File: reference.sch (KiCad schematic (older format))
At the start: 8 parts, among them U6 REF5040, U7 REF5050

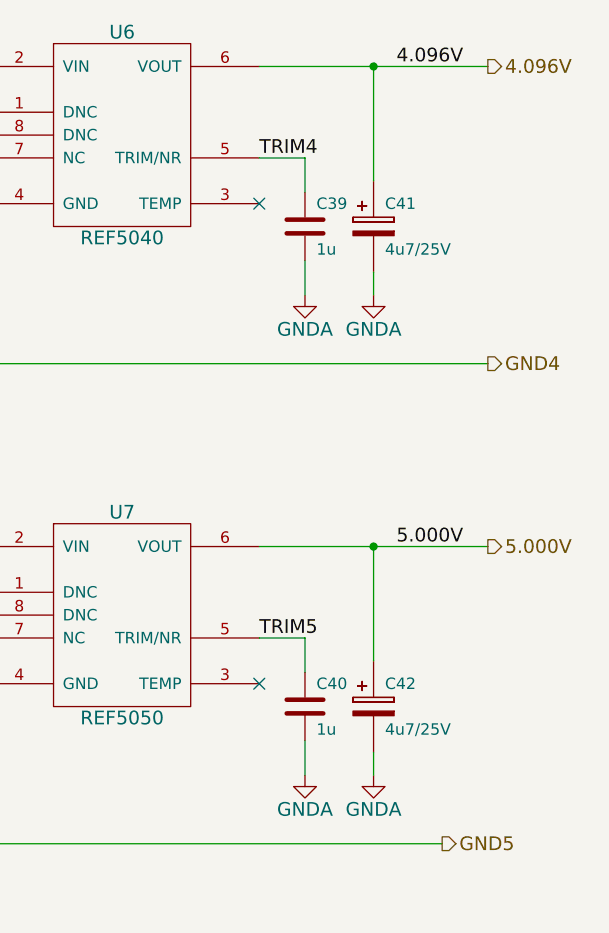
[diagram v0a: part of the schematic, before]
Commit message: Updated all part descriptions
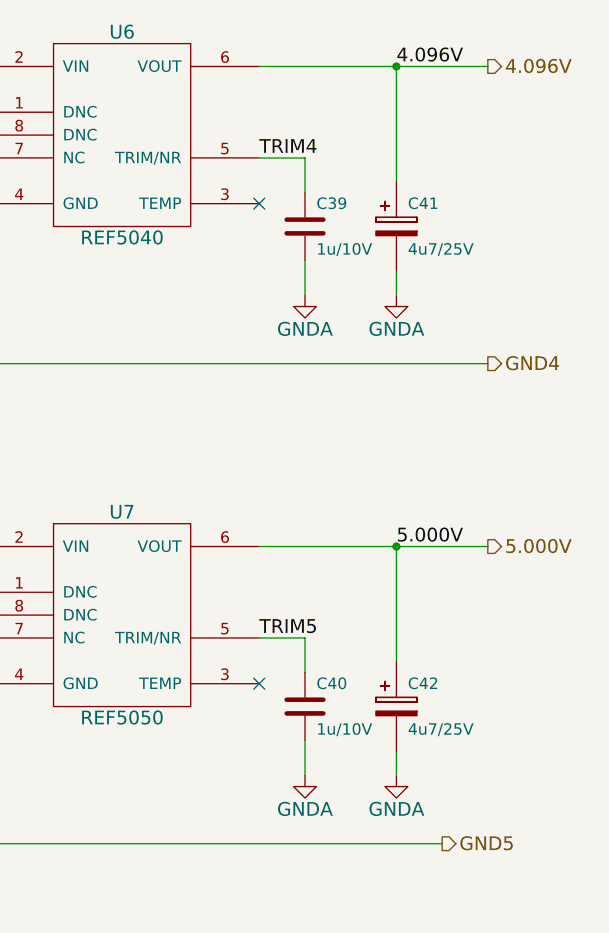
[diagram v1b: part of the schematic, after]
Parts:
- C37, C38, C41, C42: Alt. Order Code (none) -> 74-TR3B475K025C0700; Alt. Supplier (none) -> Mouser; Note (none) -> 4.7μ/25V/0.7Ω ESR case B tantalum capacitor; Package (none) -> case B; Supplier (none) -> Farnell
- C39, C40: value 1u -> 1u/10V; Alt. Order Code (none) -> 710-885012106010; Alt. Supplier (none) -> Mouser; Note (none) -> 1μF/10V X5R 0603 ceramic capacitor; Package (none) -> 0603; Supplier (none) -> Farnell
- U6: Alt. Order Code (none) -> 595-REF5040AIDGKT; Alt. Supplier (none) -> Mouser; Note (none) -> 5.000V low-noise very low drift precision voltage reference; Package (none) -> MSOP-8; Supplier (none) -> Farnell
- U7: Alt. Order Code (none) -> 595-REF5050AIDGKT; Alt. Supplier (none) -> Mouser; Note (none) -> 4.096V low-noise very low drift precision voltage reference; Package (none) -> MSOP-8; Supplier (none) -> Farnell
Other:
- moved on the sheet: C41, C42
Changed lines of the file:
@@
 EESchema Schematic File Version 2
-LIBS:MicroFLiC_DAC_1_0-rescue
 LIBS:power
 LIBS:device
@@
 LIBS:valves
 LIBS:jakub
-LIBS:MicroFLiC_DAC_1_0-cache
+LIBS:MicroFLiC_DAC-cache
 EELAYER 25 0
 EELAYER END
@@
 F 4 "REF5040AIDGKT" H 4100 2300 60  0001 C CNN "Part Number"
 F 5 "Texas Instruments" H 4100 2300 60  0001 C CNN "Manufacturer"
-F 6 "2323788" H 4100 2300 60  0001 C CNN "Order Code"
+F 6 "MSOP-8" H 4100 2300 60  0001 C CNN "Package"
+F 7 "Farnell" H 4100 2300 60  0001 C CNN "Supplier"
+F 8 "2323788" H 4100 2300 60  0001 C CNN "Order Code"
+F 9 "Mouser" H 4100 2300 60  0001 C CNN "Alt. Supplier"
+F 10 "595-REF5040AIDGKT" H 4100 2300 60  0001 C CNN "Alt. Order Code"
+F 11 "5.000V low-noise very low drift precision voltage reference" H 4100 2300 60  0001 C CNN "Note"
 	1    4100 2300
 	1    0    0    -1
@@
 AR Path="/5573B13F/5573B996" Ref="C39"  Part="1"
 F 0 "C39" H 4950 2800 50  0000 L CNN
-F 1 "1u" H 4950 2600 50  0000 L CNN
+F 1 "1u/10V" H 4950 2600 50  0000 L CNN
 F 2 "Capacitors_SMD:C_0603" H 4938 2550 30  0001 C CNN
 F 3 "" H 4900 2700 60  0000 C CNN
 F 4 "MC0603X105K100CT" H 4900 2700 60  0001 C CNN "Part Number"
 F 5 "Multicomp" H 4900 2700 60  0001 C CNN "Manufacturer"
-F 6 "1759399" H 4900 2700 60  0001 C CNN "Order Code"
+F 6 "0603" H 4900 2700 60  0001 C CNN "Package"
+F 7 "Farnell" H 4900 2700 60  0001 C CNN "Supplier"
+F 8 "1759399" H 4900 2700 60  0001 C CNN "Order Code"
+F 9 "Mouser" H 4900 2700 60  0001 C CNN "Alt. Supplier"
+F 10 "710-885012106010" H 4900 2700 60  0001 C CNN "Alt. Order Code"
+F 11 "1μF/10V X5R 0603 ceramic capacitor" H 4900 2700 60  0001 C CNN "Note"
 	1    4900 2700
 	1    0    0    -1
@@
 $EndComp
 Wire Wire Line
-	5200 2500 5200 2000
+	5300 2500 5300 2000
 Wire Wire Line
 	4700 2000 5700 2000
 Wire Wire Line
-	5200 2900 5200 3000
+	5300 2900 5300 3000
 Wire Wire Line
 	4900 3000 4900 2850
@@
 L GNDA #PWR049
 U 1 1 5573B9C2
-P 5200 3000
-F 0 "#PWR049" H 5200 2750 60  0001 C CNN
-F 1 "GNDA" H 5200 2850 60  0000 C CNN
-F 2 "" H 5200 3000 60  0000 C CNN
-F 3 "" H 5200 3000 60  0000 C CNN
-	1    5200 3000
+P 5300 3000
+F 0 "#PWR049" H 5300 2750 60  0001 C CNN
+F 1 "GNDA" H 5300 2850 60  0000 C CNN
+F 2 "" H 5300 3000 60  0000 C CNN
+F 3 "" H 5300 3000 60  0000 C CNN
+	1    5300 3000
 	1    0    0    -1
 $EndComp
@@
 F 4 "REF5050AIDGKT" H 4100 4400 60  0001 C CNN "Part Number"
 F 5 "Texas Instruments" H 4100 4400 60  0001 C CNN "Manufacturer"
-F 6 "2323802" H 4100 4400 60  0001 C CNN "Order Code"
+F 6 "MSOP-8" H 4100 4400 60  0001 C CNN "Package"
+F 7 "Farnell" H 4100 4400 60  0001 C CNN "Supplier"
+F 8 "2323802" H 4100 4400 60  0001 C CNN "Order Code"
+F 9 "Mouser" H 4100 4400 60  0001 C CNN "Alt. Supplier"
+F 10 "595-REF5050AIDGKT" H 4100 4400 60  0001 C CNN "Alt. Order Code"
+F 11 "4.096V low-noise very low drift precision voltage reference" H 4100 4400 60  0001 C CNN "Note"
 	1    4100 4400
 	1    0    0    -1
@@
 AR Path="/5573B13F/5573BE4D" Ref="C40"  Part="1"
 F 0 "C40" H 4950 4900 50  0000 L CNN
-F 1 "1u" H 4950 4700 50  0000 L CNN
+F 1 "1u/10V" H 4950 4700 50  0000 L CNN
 F 2 "Capacitors_SMD:C_0603" H 4938 4650 30  0001 C CNN
 F 3 "" H 4900 4800 60  0000 C CNN
 F 4 "MC0603X105K100CT" H 4900 4800 60  0001 C CNN "Part Number"
 F 5 "Multicomp" H 4900 4800 60  0001 C CNN "Manufacturer"
-F 6 "1759399" H 4900 4800 60  0001 C CNN "Order Code"
+F 6 "0603" H 4900 4800 60  0001 C CNN "Package"
+F 7 "Farnell" H 4900 4800 60  0001 C CNN "Supplier"
+F 8 "1759399" H 4900 4800 60  0001 C CNN "Order Code"
+F 9 "Mouser" H 4900 4800 60  0001 C CNN "Alt. Supplier"
+F 10 "710-885012106010" H 4900 4800 60  0001 C CNN "Alt. Order Code"
+F 11 "1μF/10V X5R 0603 ceramic capacitor" H 4900 4800 60  0001 C CNN "Note"
 	1    4900 4800
 	1    0    0    -1
@@
 $EndComp
 Wire Wire Line
-	5200 4600 5200 4100
+	5300 4600 5300 4100
 Wire Wire Line
 	4700 4100 5700 4100
 Wire Wire Line
-	5200 5000 5200 5100
+	5300 5000 5300 5100
 Wire Wire Line
 	4900 5100 4900 4950
@@
 L GNDA #PWR052
 U 1 1 5573BE72
-P 5200 5100
-F 0 "#PWR052" H 5200 4850 60  0001 C CNN
-F 1 "GNDA" H 5200 4950 60  0000 C CNN
-F 2 "" H 5200 5100 60  0000 C CNN
-F 3 "" H 5200 5100 60  0000 C CNN
-	1    5200 5100
+P 5300 5100
+F 0 "#PWR052" H 5300 4850 60  0001 C CNN
+F 1 "GNDA" H 5300 4950 60  0000 C CNN
+F 2 "" H 5300 5100 60  0000 C CNN
+F 3 "" H 5300 5100 60  0000 C CNN
+	1    5300 5100
 	1    0    0    -1
 $EndComp
@@
 	2700 2000 2700 4100
 Connection ~ 2700 2000
-Connection ~ 5200 2000
-Connection ~ 5200 4100
+Connection ~ 5300 2000
+Connection ~ 5300 4100
 Text HLabel 5700 2000 2    60   Output ~ 0
 4.096V
@@
 F 4 "TR3B475K025C0700" H 2900 2700 60  0001 C CNN "Part Number"
 F 5 "Vishay" H 2900 2700 60  0001 C CNN "Manufacturer"
-F 6 "2353145" H 2900 2700 60  0001 C CNN "Order Code"
+F 6 "case B" H 2900 2700 60  0001 C CNN "Package"
+F 7 "Farnell" H 2900 2700 60  0001 C CNN "Supplier"
+F 8 "2353145" H 2900 2700 60  0001 C CNN "Order Code"
+F 9 "Mouser" H 2900 2700 60  0001 C CNN "Alt. Supplier"
+F 10 "74-TR3B475K025C0700" H 2900 2700 60  0001 C CNN "Alt. Order Code"
+F 11 "4.7μ/25V/0.7Ω ESR case B tantalum capacitor" H 2900 2700 60  0001 C CNN "Note"
 	1    2900 2700
 	1    0    0    -1
@@
 F 4 "TR3B475K025C0700" H 2900 4800 60  0001 C CNN "Part Number"
 F 5 "Vishay" H 2900 4800 60  0001 C CNN "Manufacturer"
-F 6 "2353145" H 2900 4800 60  0001 C CNN "Order Code"
+F 6 "case B" H 2900 4800 60  0001 C CNN "Package"
+F 7 "Farnell" H 2900 4800 60  0001 C CNN "Supplier"
+F 8 "2353145" H 2900 4800 60  0001 C CNN "Order Code"
+F 9 "Mouser" H 2900 4800 60  0001 C CNN "Alt. Supplier"
+F 10 "74-TR3B475K025C0700" H 2900 4800 60  0001 C CNN "Alt. Order Code"
+F 11 "4.7μ/25V/0.7Ω ESR case B tantalum capacitor" H 2900 4800 60  0001 C CNN "Note"
 	1    2900 4800
 	1    0    0    -1
@@
 L CP2 C42
 U 1 1 5574D196
-P 5200 4800
-F 0 "C42" H 5250 4900 50  0000 L CNN
-F 1 "4u7/25V" H 5250 4700 50  0000 L CNN
-F 2 "Capacitors_Tantalum_SMD:TantalC_SizeB_EIA-3528_Reflow" H 5238 4650 30  0001 C CNN
-F 3 "" H 5200 4800 60  0000 C CNN
-F 4 "TR3B475K025C0700" H 5200 4800 60  0001 C CNN "Part Number"
-F 5 "Vishay" H 5200 4800 60  0001 C CNN "Manufacturer"
-F 6 "2353145" H 5200 4800 60  0001 C CNN "Order Code"
-	1    5200 4800
+P 5300 4800
+F 0 "C42" H 5350 4900 50  0000 L CNN
+F 1 "4u7/25V" H 5350 4700 50  0000 L CNN
+F 2 "Capacitors_Tantalum_SMD:TantalC_SizeB_EIA-3528_Reflow" H 5338 4650 30  0001 C CNN
+F 3 "" H 5300 4800 60  0000 C CNN
+F 4 "TR3B475K025C0700" H 5300 4800 60  0001 C CNN "Part Number"
+F 5 "Vishay" H 5300 4800 60  0001 C CNN "Manufacturer"
+F 6 "case B" H 5300 4800 60  0001 C CNN "Package"
+F 7 "Farnell" H 5300 4800 60  0001 C CNN "Supplier"
+F 8 "2353145" H 5300 4800 60  0001 C CNN "Order Code"
+F 9 "Mouser" H 5300 4800 60  0001 C CNN "Alt. Supplier"
+F 10 "74-TR3B475K025C0700" H 5300 4800 60  0001 C CNN "Alt. Order Code"
+F 11 "4.7μ/25V/0.7Ω ESR case B tantalum capacitor" H 5300 4800 60  0001 C CNN "Note"
+	1    5300 4800
 	1    0    0    -1
 $EndComp
@@
 L CP2 C41
 U 1 1 5574D236
-P 5200 2700
-F 0 "C41" H 5250 2800 50  0000 L CNN
-F 1 "4u7/25V" H 5250 2600 50  0000 L CNN
-F 2 "Capacitors_Tantalum_SMD:TantalC_SizeB_EIA-3528_Reflow" H 5238 2550 30  0001 C CNN
-F 3 "" H 5200 2700 60  0000 C CNN
-F 4 "TR3B475K025C0700" H 5200 2700 60  0001 C CNN "Part Number"
-F 5 "Vishay" H 5200 2700 60  0001 C CNN "Manufacturer"
-F 6 "2353145" H 5200 2700 60  0001 C CNN "Order Code"
-	1    5200 2700
-	1    0    0    -1
-$EndComp
+P 5300 2700
+F 0 "C41" H 5350 2800 50  0000 L CNN
+F 1 "4u7/25V" H 5350 2600 50  0000 L CNN
+F 2 "Capacitors_Tantalum_SMD:TantalC_SizeB_EIA-3528_Reflow" H 5338 2550 30  0001 C CNN
+F 3 "" H 5300 2700 60  0000 C CNN
+F 4 "TR3B475K025C0700" H 5300 2700 60  0001 C CNN "Part Number"
+F 5 "Vishay" H 5300 2700 60  0001 C CNN "Manufacturer"
+F 6 "case B" H 5300 2700 60  0001 C CNN "Package"
+F 7 "Farnell" H 5300 2700 60  0001 C CNN "Supplier"
+F 8 "2353145" H 5300 2700 60  0001 C CNN "Order Code"
+F 9 "Mouser" H 5300 2700 60  0001 C CNN "Alt. Supplier"
+F 10 "74-TR3B475K025C0700" H 5300 2700 60  0001 C CNN "Alt. Order Code"
+F 11 "4.7μ/25V/0.7Ω ESR case B tantalum capacitor" H 5300 2700 60  0001 C CNN "Note"
+	1    5300 2700
+	1    0    0    -1
+$EndComp

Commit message: Fixed ground problems, added bypass capacitors, added resistor between digital isolator and DAC
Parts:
- removed C37, C38, C41, C42: 4u7/25V, Capacitors_Tantalum_SMD:TantalC_SizeB_EIA-3528_Reflow, symbol CP2
- added C45, C46, C49, C50: 22u/25V, Capacitors_SMD:C_1210, symbol C
- added R10, R11: 1, Resistors_SMD:R_0805, symbol R
- renumbered C39 to C47, C40 to C48
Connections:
- net 4.096V: now also R10.1
- net 5.000V: now also R11.1
- net GNDA: now also C45.2, C46.2, C49.2, C50.2
- net VREF: now also C45.1, C46.1
- new net: C49.1, R10.2
- new net: C50.1, R11.2
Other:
- note added: "1Ω ESR resistor for output stability"
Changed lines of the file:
@@
 $EndComp
 $Comp
-L C C39
+L C C47
 U 1 1 5573B996
 P 4900 2700
-AR Path="/5573B996" Ref="C39"  Part="1"
-AR Path="/5573B13F/5573B996" Ref="C39"  Part="1"
-F 0 "C39" H 4950 2800 50  0000 L CNN
+F 0 "C47" H 4950 2800 50  0000 L CNN
 F 1 "1u/10V" H 4950 2600 50  0000 L CNN
 F 2 "Capacitors_SMD:C_0603" H 4938 2550 30  0001 C CNN
@@
 	2200 2000 3500 2000
 Wire Wire Line
-	2900 2000 2900 2500
-$Comp
-L GNDA #PWR047
+	2900 2000 2900 2600
+$Comp
+L GNDA #PWR045
 U 1 1 5573B9A8
 P 2900 3000
-F 0 "#PWR047" H 2900 2750 60  0001 C CNN
+F 0 "#PWR045" H 2900 2750 60  0001 C CNN
 F 1 "GNDA" H 2900 2850 60  0000 C CNN
 F 2 "" H 2900 3000 60  0000 C CNN
@@
 $EndComp
 $Comp
-L GNDA #PWR048
+L GNDA #PWR046
 U 1 1 5573B9AE
 P 4900 3000
-F 0 "#PWR048" H 4900 2750 60  0001 C CNN
+F 0 "#PWR046" H 4900 2750 60  0001 C CNN
 F 1 "GNDA" H 4900 2850 60  0000 C CNN
 F 2 "" H 4900 3000 60  0000 C CNN
@@
 $EndComp
 Wire Wire Line
-	5300 2500 5300 2000
+	5300 2150 5300 2000
 Wire Wire Line
 	4700 2000 5700 2000
 Wire Wire Line
-	5300 2900 5300 3000
+	5300 2850 5300 3000
 Wire Wire Line
 	4900 3000 4900 2850
@@
 	2900 3000 2900 2900
 $Comp
-L GNDA #PWR049
+L GNDA #PWR047
 U 1 1 5573B9C2
 P 5300 3000
-F 0 "#PWR049" H 5300 2750 60  0001 C CNN
+F 0 "#PWR047" H 5300 2750 60  0001 C CNN
 F 1 "GNDA" H 5300 2850 60  0000 C CNN
 F 2 "" H 5300 3000 60  0000 C CNN
@@
 $EndComp
 $Comp
-L C C40
+L C C48
 U 1 1 5573BE4D
 P 4900 4800
-AR Path="/5573BE4D" Ref="C40"  Part="1"
-AR Path="/5573B13F/5573BE4D" Ref="C40"  Part="1"
-F 0 "C40" H 4950 4900 50  0000 L CNN
+F 0 "C48" H 4950 4900 50  0000 L CNN
 F 1 "1u/10V" H 4950 4700 50  0000 L CNN
 F 2 "Capacitors_SMD:C_0603" H 4938 4650 30  0001 C CNN
@@
 	2700 4100 3500 4100
 Wire Wire Line
-	2900 4100 2900 4600
-$Comp
-L GNDA #PWR050
+	2900 4100 2900 4700
+$Comp
+L GNDA #PWR048
 U 1 1 5573BE5B
 P 2900 5100
-F 0 "#PWR050" H 2900 4850 60  0001 C CNN
+F 0 "#PWR048" H 2900 4850 60  0001 C CNN
 F 1 "GNDA" H 2900 4950 60  0000 C CNN
 F 2 "" H 2900 5100 60  0000 C CNN
@@
 $EndComp
 $Comp
-L GNDA #PWR051
+L GNDA #PWR049
 U 1 1 5573BE61
 P 4900 5100
-F 0 "#PWR051" H 4900 4850 60  0001 C CNN
+F 0 "#PWR049" H 4900 4850 60  0001 C CNN
 F 1 "GNDA" H 4900 4950 60  0000 C CNN
 F 2 "" H 4900 5100 60  0000 C CNN
@@
 $EndComp
 Wire Wire Line
-	5300 4600 5300 4100
+	5300 4250 5300 4100
 Wire Wire Line
 	4700 4100 5700 4100
 Wire Wire Line
-	5300 5000 5300 5100
+	5300 4950 5300 5100
 Wire Wire Line
 	4900 5100 4900 4950
@@
 	2900 5100 2900 5000
 $Comp
-L GNDA #PWR052
+L GNDA #PWR050
 U 1 1 5573BE72
 P 5300 5100
-F 0 "#PWR052" H 5300 4850 60  0001 C CNN
+F 0 "#PWR050" H 5300 4850 60  0001 C CNN
 F 1 "GNDA" H 5300 4950 60  0000 C CNN
 F 2 "" H 5300 5100 60  0000 C CNN
@@
 	3400 2600 3400 3400
 $Comp
-L GNDA #PWR053
+L GNDA #PWR051
 U 1 1 5573C48B
 P 3400 3400
-F 0 "#PWR053" H 3400 3150 60  0001 C CNN
+F 0 "#PWR051" H 3400 3150 60  0001 C CNN
 F 1 "GNDA" H 3400 3250 60  0000 C CNN
 F 2 "" H 3400 3400 60  0000 C CNN
@@
 	3400 4700 3400 5500
 $Comp
-L GNDA #PWR054
+L GNDA #PWR052
 U 1 1 5573C579
 P 3400 5500
-F 0 "#PWR054" H 3400 5250 60  0001 C CNN
+F 0 "#PWR052" H 3400 5250 60  0001 C CNN
 F 1 "GNDA" H 3400 5350 60  0000 C CNN
 F 2 "" H 3400 5500 60  0000 C CNN
@@
 GND5
 $Comp
-L CP2 C37
-U 1 1 5574CCB3
-P 2900 2700
-F 0 "C37" H 2950 2800 50  0000 L CNN
-F 1 "4u7/25V" H 2950 2600 50  0000 L CNN
-F 2 "Capacitors_Tantalum_SMD:TantalC_SizeB_EIA-3528_Reflow" H 2938 2550 30  0001 C CNN
-F 3 "" H 2900 2700 60  0000 C CNN
-F 4 "TR3B475K025C0700" H 2900 2700 60  0001 C CNN "Part Number"
-F 5 "Vishay" H 2900 2700 60  0001 C CNN "Manufacturer"
-F 6 "case B" H 2900 2700 60  0001 C CNN "Package"
-F 7 "Farnell" H 2900 2700 60  0001 C CNN "Supplier"
-F 8 "2353145" H 2900 2700 60  0001 C CNN "Order Code"
-F 9 "Mouser" H 2900 2700 60  0001 C CNN "Alt. Supplier"
-F 10 "74-TR3B475K025C0700" H 2900 2700 60  0001 C CNN "Alt. Order Code"
-F 11 "4.7μ/25V/0.7Ω ESR case B tantalum capacitor" H 2900 2700 60  0001 C CNN "Note"
-	1    2900 2700
-	1    0    0    -1
-$EndComp
-$Comp
-L CP2 C38
-U 1 1 5574D13E
-P 2900 4800
-F 0 "C38" H 2950 4900 50  0000 L CNN
-F 1 "4u7/25V" H 2950 4700 50  0000 L CNN
-F 2 "Capacitors_Tantalum_SMD:TantalC_SizeB_EIA-3528_Reflow" H 2938 4650 30  0001 C CNN
-F 3 "" H 2900 4800 60  0000 C CNN
-F 4 "TR3B475K025C0700" H 2900 4800 60  0001 C CNN "Part Number"
-F 5 "Vishay" H 2900 4800 60  0001 C CNN "Manufacturer"
-F 6 "case B" H 2900 4800 60  0001 C CNN "Package"
-F 7 "Farnell" H 2900 4800 60  0001 C CNN "Supplier"
-F 8 "2353145" H 2900 4800 60  0001 C CNN "Order Code"
-F 9 "Mouser" H 2900 4800 60  0001 C CNN "Alt. Supplier"
-F 10 "74-TR3B475K025C0700" H 2900 4800 60  0001 C CNN "Alt. Order Code"
-F 11 "4.7μ/25V/0.7Ω ESR case B tantalum capacitor" H 2900 4800 60  0001 C CNN "Note"
-	1    2900 4800
-	1    0    0    -1
-$EndComp
-$Comp
-L CP2 C42
-U 1 1 5574D196
+L C C45
+U 1 1 56E01DBE
+P 2900 2750
+F 0 "C45" H 2950 2850 50  0000 L CNN
+F 1 "22u/25V" H 2950 2650 50  0000 L CNN
+F 2 "Capacitors_SMD:C_1210" H 2938 2600 30  0001 C CNN
+F 3 "" H 2900 2750 60  0000 C CNN
+F 4 "GRM32ER61E226ME15L" H 2900 2750 60  0001 C CNN "Part Number"
+F 5 "Murata" H 2900 2750 60  0001 C CNN "Manufacturer"
+F 6 "1210" H 2900 2750 60  0001 C CNN "Package"
+F 7 "Farnell" H 2900 2750 60  0001 C CNN "Supplier"
+F 8 "1735539" H 2900 2750 60  0001 C CNN "Order Code"
+F 9 "Mouser" H 2900 2750 60  0001 C CNN "Alt. Supplier"
+F 10 "81-GRM32ER61E226ME5L" H 2900 2750 60  0001 C CNN "Alt. Order Code"
+F 11 "22μF/25V X5R 1210 ceramic capacitor" H 2900 2750 60  0001 C CNN "Note"
+	1    2900 2750
+	1    0    0    -1
+$EndComp
+$Comp
+L C C46
+U 1 1 56E01F62
+P 2900 4850
+F 0 "C46" H 2950 4950 50  0000 L CNN
+F 1 "22u/25V" H 2950 4750 50  0000 L CNN
+F 2 "Capacitors_SMD:C_1210" H 2938 4700 30  0001 C CNN
+F 3 "" H 2900 4850 60  0000 C CNN
+F 4 "GRM32ER61E226ME15L" H 2900 4850 60  0001 C CNN "Part Number"
+F 5 "Murata" H 2900 4850 60  0001 C CNN "Manufacturer"
+F 6 "1210" H 2900 4850 60  0001 C CNN "Package"
+F 7 "Farnell" H 2900 4850 60  0001 C CNN "Supplier"
+F 8 "1735539" H 2900 4850 60  0001 C CNN "Order Code"
+F 9 "Mouser" H 2900 4850 60  0001 C CNN "Alt. Supplier"
+F 10 "81-GRM32ER61E226ME5L" H 2900 4850 60  0001 C CNN "Alt. Order Code"
+F 11 "22μF/25V X5R 1210 ceramic capacitor" H 2900 4850 60  0001 C CNN "Note"
+	1    2900 4850
+	1    0    0    -1
+$EndComp
+$Comp
+L C C49
+U 1 1 56E020B8
+P 5300 2700
+F 0 "C49" H 5350 2800 50  0000 L CNN
+F 1 "22u/25V" H 5350 2600 50  0000 L CNN
+F 2 "Capacitors_SMD:C_1210" H 5338 2550 30  0001 C CNN
+F 3 "" H 5300 2700 60  0000 C CNN
+F 4 "GRM32ER61E226ME15L" H 5300 2700 60  0001 C CNN "Part Number"
+F 5 "Murata" H 5300 2700 60  0001 C CNN "Manufacturer"
+F 6 "1210" H 5300 2700 60  0001 C CNN "Package"
+F 7 "Farnell" H 5300 2700 60  0001 C CNN "Supplier"
+F 8 "1735539" H 5300 2700 60  0001 C CNN "Order Code"
+F 9 "Mouser" H 5300 2700 60  0001 C CNN "Alt. Supplier"
+F 10 "81-GRM32ER61E226ME5L" H 5300 2700 60  0001 C CNN "Alt. Order Code"
+F 11 "22μF/25V X5R 1210 ceramic capacitor" H 5300 2700 60  0001 C CNN "Note"
+	1    5300 2700
+	1    0    0    -1
+$EndComp
+$Comp
+L C C50
+U 1 1 56E0213B
 P 5300 4800
-F 0 "C42" H 5350 4900 50  0000 L CNN
-F 1 "4u7/25V" H 5350 4700 50  0000 L CNN
-F 2 "Capacitors_Tantalum_SMD:TantalC_SizeB_EIA-3528_Reflow" H 5338 4650 30  0001 C CNN
+F 0 "C50" H 5350 4900 50  0000 L CNN
+F 1 "22u/25V" H 5350 4700 50  0000 L CNN
+F 2 "Capacitors_SMD:C_1210" H 5338 4650 30  0001 C CNN
 F 3 "" H 5300 4800 60  0000 C CNN
-F 4 "TR3B475K025C0700" H 5300 4800 60  0001 C CNN "Part Number"
-F 5 "Vishay" H 5300 4800 60  0001 C CNN "Manufacturer"
-F 6 "case B" H 5300 4800 60  0001 C CNN "Package"
+F 4 "GRM32ER61E226ME15L" H 5300 4800 60  0001 C CNN "Part Number"
+F 5 "Murata" H 5300 4800 60  0001 C CNN "Manufacturer"
+F 6 "1210" H 5300 4800 60  0001 C CNN "Package"
 F 7 "Farnell" H 5300 4800 60  0001 C CNN "Supplier"
-F 8 "2353145" H 5300 4800 60  0001 C CNN "Order Code"
+F 8 "1735539" H 5300 4800 60  0001 C CNN "Order Code"
 F 9 "Mouser" H 5300 4800 60  0001 C CNN "Alt. Supplier"
-F 10 "74-TR3B475K025C0700" H 5300 4800 60  0001 C CNN "Alt. Order Code"
-F 11 "4.7μ/25V/0.7Ω ESR case B tantalum capacitor" H 5300 4800 60  0001 C CNN "Note"
+F 10 "81-GRM32ER61E226ME5L" H 5300 4800 60  0001 C CNN "Alt. Order Code"
+F 11 "22μF/25V X5R 1210 ceramic capacitor" H 5300 4800 60  0001 C CNN "Note"
 	1    5300 4800
 	1    0    0    -1
 $EndComp
 $Comp
-L CP2 C41
-U 1 1 5574D236
-P 5300 2700
-F 0 "C41" H 5350 2800 50  0000 L CNN
-F 1 "4u7/25V" H 5350 2600 50  0000 L CNN
-F 2 "Capacitors_Tantalum_SMD:TantalC_SizeB_EIA-3528_Reflow" H 5338 2550 30  0001 C CNN
-F 3 "" H 5300 2700 60  0000 C CNN
-F 4 "TR3B475K025C0700" H 5300 2700 60  0001 C CNN "Part Number"
-F 5 "Vishay" H 5300 2700 60  0001 C CNN "Manufacturer"
-F 6 "case B" H 5300 2700 60  0001 C CNN "Package"
-F 7 "Farnell" H 5300 2700 60  0001 C CNN "Supplier"
-F 8 "2353145" H 5300 2700 60  0001 C CNN "Order Code"
-F 9 "Mouser" H 5300 2700 60  0001 C CNN "Alt. Supplier"
-F 10 "74-TR3B475K025C0700" H 5300 2700 60  0001 C CNN "Alt. Order Code"
-F 11 "4.7μ/25V/0.7Ω ESR case B tantalum capacitor" H 5300 2700 60  0001 C CNN "Note"
-	1    5300 2700
-	1    0    0    -1
-$EndComp
+L R R10
+U 1 1 56E021C3
+P 5300 2300
+F 0 "R10" V 5380 2300 50  0000 C CNN
+F 1 "1" V 5300 2300 50  0000 C CNN
+F 2 "Resistors_SMD:R_0805" V 5230 2300 50  0001 C CNN
+F 3 "" H 5300 2300 50  0000 C CNN
+	1    5300 2300
+	1    0    0    -1
+$EndComp
+Wire Wire Line
+	5300 2550 5300 2450
+$Comp
+L R R11
+U 1 1 56E02322
+P 5300 4400
+F 0 "R11" V 5380 4400 50  0000 C CNN
+F 1 "1" V 5300 4400 50  0000 C CNN
+F 2 "Resistors_SMD:R_0805" V 5230 4400 50  0001 C CNN
+F 3 "" H 5300 4400 50  0000 C CNN
+	1    5300 4400
+	1    0    0    -1
+$EndComp
+Wire Wire Line
+	5300 4650 5300 4550
+Text Notes 5650 2350 0    60   ~ 0
+1Ω ESR resistor for output stability
 $EndSCHEMATC
